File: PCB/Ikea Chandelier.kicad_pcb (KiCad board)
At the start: 2 copper layers, 50 x 50 mm, 23 parts, among them J1 Arduino_Pro_Mini_Header, P1 RGB12, P2 Power, P3 RGB34, P4 RS485, P5 RGB56, P6 Candles, U1 78L05, U2 MAX485

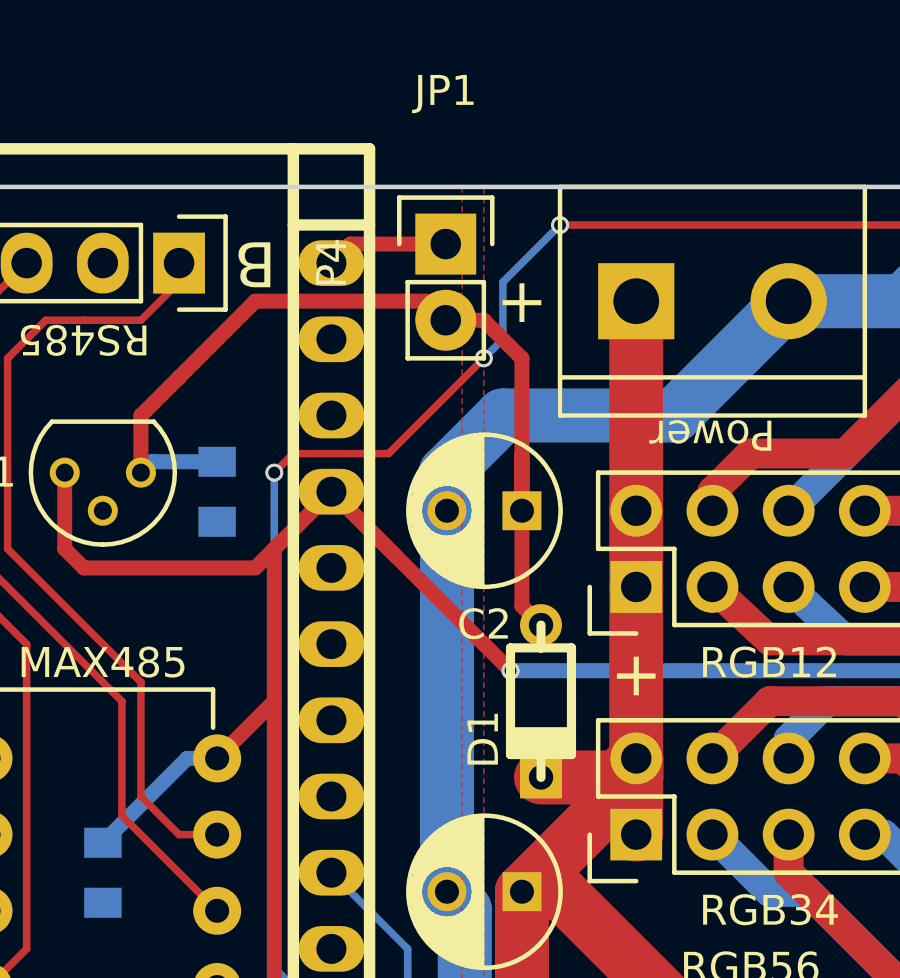
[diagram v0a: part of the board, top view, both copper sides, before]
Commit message: SMD jumper + code testing
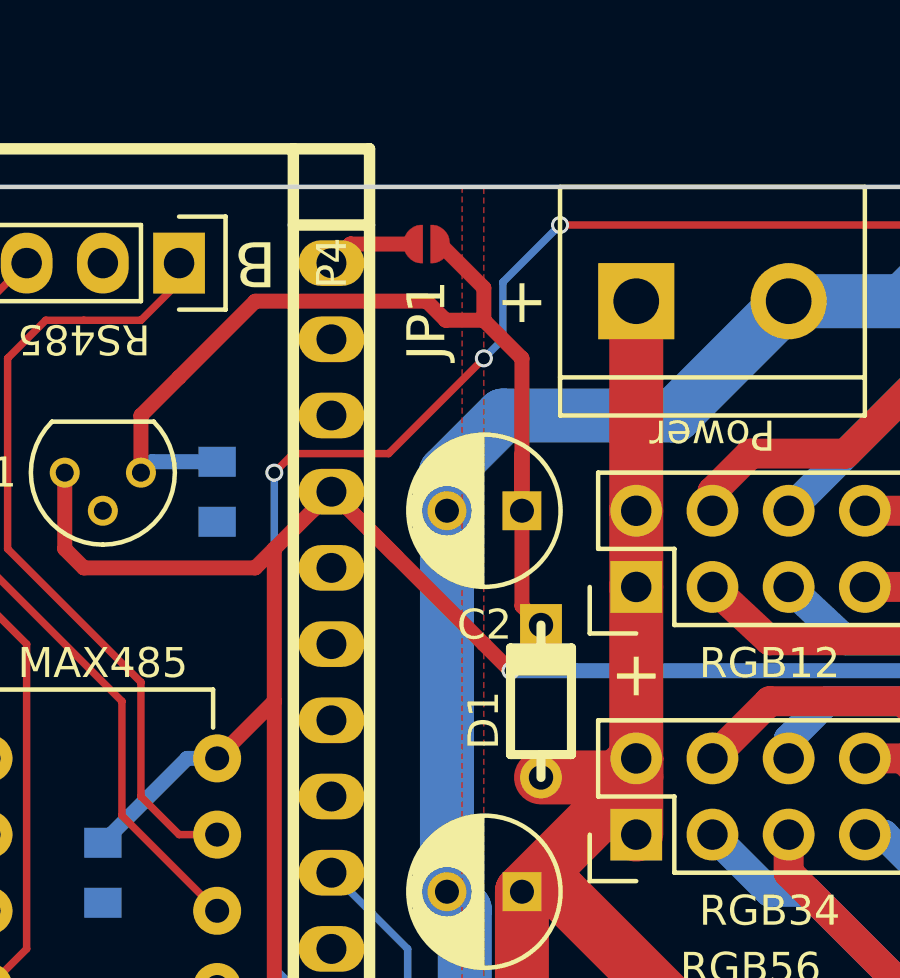
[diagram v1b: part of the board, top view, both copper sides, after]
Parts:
- JP1: footprint Pin_Headers:Pin_Header_Straight_1x02 -> septillion_device:SMD_jumper2
- moved JP1 0.64 mm to (90.3, 81.9)
- turned D1 to 90 degrees
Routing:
- net /Vraw: track 30.7 -> 33.9 mm
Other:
- rule pad_to_mask_clearance: 0.2 -> 0.1524

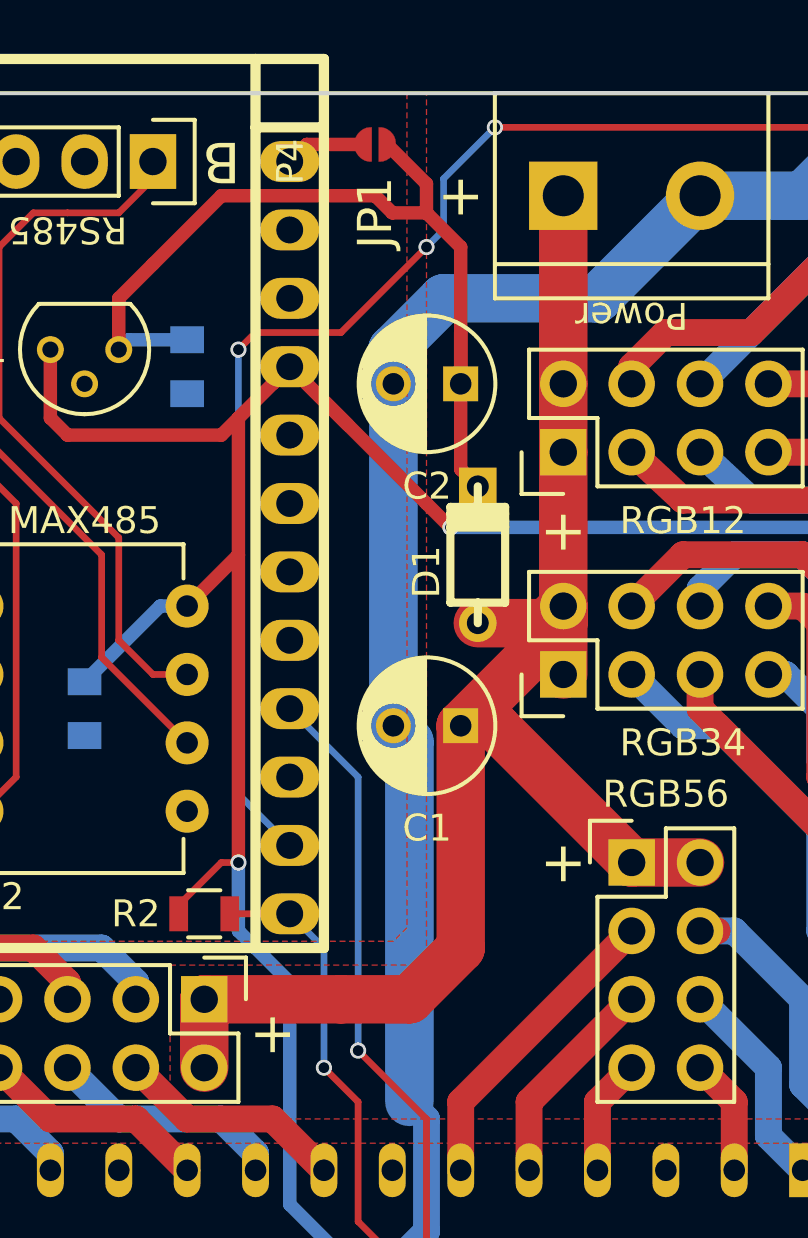
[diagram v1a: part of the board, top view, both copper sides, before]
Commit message: Diode corrected, markings fixed, ordered v1
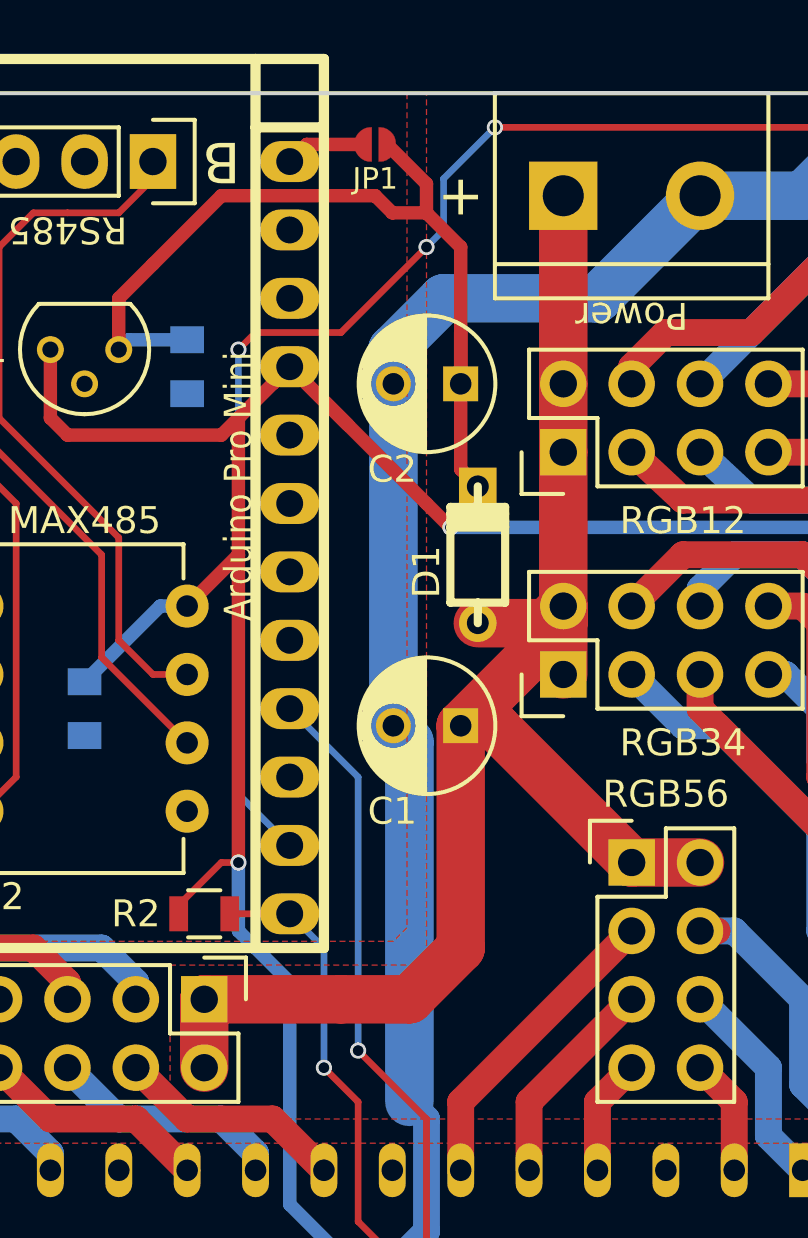
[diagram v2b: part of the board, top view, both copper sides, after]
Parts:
- J1: value Arduino_Pro_Mini_Header -> Arduino Pro Mini
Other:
- board text added: "Short JP1 and don't populate U1 to use Arduino regulator"
- board text added: "Timo Engelgeer 2016 Ikea Chandelier node v1"
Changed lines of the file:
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@@
     (links 85)
     (no_connects 0)
-    (area 69.924999 79.924999 120.075001 130.075001)
+    (area 69.924999 77.605 120.075001 130.075001)
     (thickness 1.6)
-    (drawings 12)
+    (drawings 14)
     (tracks 349)
     (zones 0)
@@
   (page A4)
   (layers
-    (0 F.Cu signal)
+    (0 F.Cu signal hide)
     (31 B.Cu signal hide)
     (32 B.Adhes user)
@@
     (34 B.Paste user)
     (35 F.Paste user)
-    (36 B.SilkS user)
+    (36 B.SilkS user hide)
     (37 F.SilkS user)
     (38 B.Mask user)
@@
     (descr "Radial Electrolytic Capacitor Diameter 5mm x Length 11mm, Pitch 2.5mm")
     (tags "Electrolytic Capacitor")
-    (fp_text reference C1 (at 1.25 -3.8 180) (layer F.SilkS)
+    (fp_text reference C1 (at 2.54 -3.175 180) (layer F.SilkS)
       (effects (font (size 1 1) (thickness 0.15)))
     )
@@
     (descr "Radial Electrolytic Capacitor Diameter 5mm x Length 11mm, Pitch 2.5mm")
     (tags "Electrolytic Capacitor")
-    (fp_text reference C2 (at 1.25 -3.8 180) (layer F.SilkS)
+    (fp_text reference C2 (at 2.54 -3.175 180) (layer F.SilkS)
       (effects (font (size 1 1) (thickness 0.15)))
     )
@@
       (effects (font (size 1.016 1.016) (thickness 0.2032)))
     )
-    (fp_text value Arduino_Pro_Mini_Header (at 0 -1.27 270) (layer F.SilkS) hide
+    (fp_text value "Arduino Pro Mini" (at -0.635 -5.715 270) (layer F.SilkS)
       (effects (font (size 1.016 0.889) (thickness 0.2032)))
     )
@@
     (descr "Through hole pin header")
     (tags "pin header")
-    (fp_text reference P4 (at 0 -5.1 270) (layer F.SilkS)
+    (fp_text reference P4 (at 0 -5.1 270) (layer F.SilkS) hide
       (effects (font (size 1 1) (thickness 0.15)))
     )
@@
     (tags "capacitor 0805")
     (attr smd)
-    (fp_text reference C3 (at -3.175 0 270) (layer B.SilkS)
+    (fp_text reference C3 (at 3.175 0 270) (layer B.SilkS)
       (effects (font (size 1 1) (thickness 0.15)) (justify mirror))
     )
@@
   (module septillion_device:SMD_jumper2 (layer F.Cu)
     (at 90.32 81.905)
-    (fp_text reference JP1 (at 0 2.54 90) (layer F.SilkS)
-      (effects (font (thickness 0.3)))
+    (fp_text reference JP1 (at 0 1.27 180) (layer F.SilkS)
+      (effects (font (size 0.8 0.8) (thickness 0.15)))
     )
     (fp_text value Jumper_NC_Small (at 3.556 6.096) (layer F.SilkS) hide
@@
     )
   )
+  (gr_text "Short JP1 and don't populate \nU1 to use Arduino regulator" (at 106.83 86.985) (layer B.SilkS)
+    (effects (font (size 1 0.8) (thickness 0.15)) (justify left mirror))
+  )
+  (gr_text "Timo Engelgeer 2016\nIkea Chandelier node v1" (at 118.895 123.815) (layer B.SilkS)
+    (effects (font (size 1.5 1.5) (thickness 0.3)) (justify left mirror))
+  )
   (gr_text A (at 74.445 82.54 180) (layer F.SilkS)
     (effects (font (size 1.5 1.5) (thickness 0.3)))
@@
     (effects (font (size 1 1) (thickness 0.15)))
   )
-  (gr_text + (at 86.51 114.925) (layer F.SilkS)
+  (gr_text + (at 86.51 114.925) (layer F.Mask)
     (effects (font (size 1.5 1.5) (thickness 0.3)))
   )
-  (gr_text + (at 97.305 108.575) (layer F.SilkS)
+  (gr_text + (at 97.305 108.575) (layer F.Mask)
     (effects (font (size 1.5 1.5) (thickness 0.3)))
   )
-  (gr_text + (at 97.305 96.256) (layer F.SilkS)
+  (gr_text + (at 97.305 96.256) (layer F.Mask)
     (effects (font (size 1.5 1.5) (thickness 0.3)))
   )
